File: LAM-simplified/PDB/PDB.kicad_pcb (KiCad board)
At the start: 2 copper layers, 115 x 115 mm, 23 parts, among them J1 2.54mm 2x3, J10 xt60-female, J11 xt60-female, J12 xt60-female, J13 xt90-female, J14 xt90-female, J15 2.54mm 2x3, J2 2.54mm 2x3, J3 2.54mm 2x3, J5 xt30-female, J6 xt30-female, J7 xt60-female, J8 xt60-female, J9 xt60-female

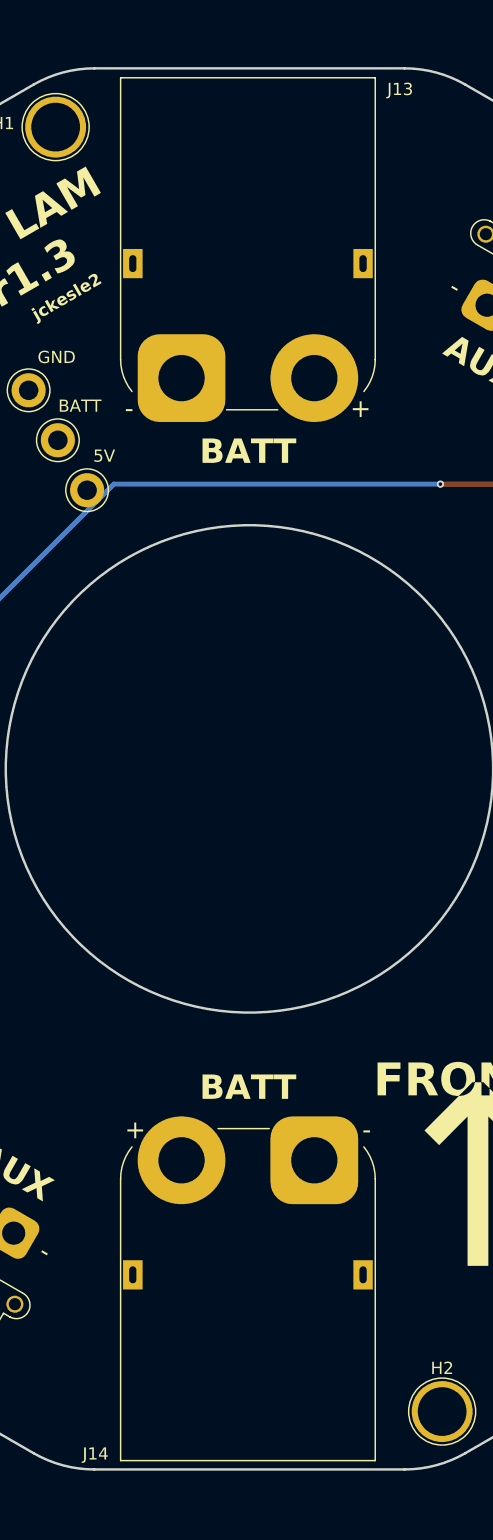
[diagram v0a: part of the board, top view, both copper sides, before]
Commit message: fix XT90-F footprint
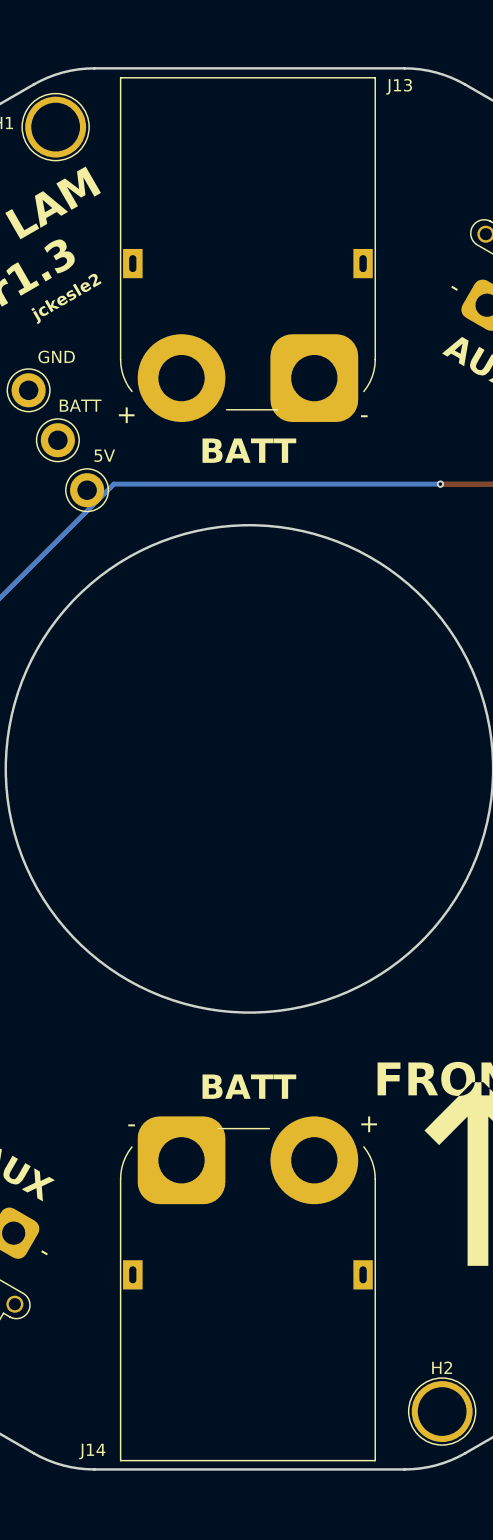
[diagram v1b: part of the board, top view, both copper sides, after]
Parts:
- J13, J14: footprint Connector_AMASS:AMASS_XT90PW-M_1x02_P10.90mm_Horizontal -> aerpaw-footprints:AMASS_XT90PW-F
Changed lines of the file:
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@@
 	(net 10 "unconnected-(J15-Pin_4-Pad4)")
 	(net 11 "unconnected-(J15-Pin_3-Pad3)")
-	(footprint "Connector_AMASS:AMASS_XT90PW-M_1x02_P10.90mm_Horizontal"
+	(footprint "aerpaw-footprints:AMASS_XT90PW-F"
 		(layer "F.Cu")
 		(at 158.25 65.5)
@@
 		(tags "RC")
 		(property "Reference" "J13"
-			(at 17.95 -23.7 0)
+			(at 17.95 -24 0)
 			(layer "F.SilkS")
 			(effects
@@
 			)
 		)
-		(property "Datasheet" "~"
+		(property "Datasheet" ""
 			(at 0 0 0)
 			(unlocked yes)
@@
 			)
 		)
-		(property "Description" "https://www.lcsc.com/product-detail/C3040690.html"
+		(property "Description" ""
 			(at 0 0 0)
 			(unlocked yes)
@@
 		)
 		(fp_text user "-"
-			(at -4.3 2.5 0)
+			(at 15 3 0)
 			(layer "F.SilkS")
 			(effects
@@
 		)
 		(fp_text user "+"
-			(at 14.7 2.5 0)
+			(at -4.5 3 0)
 			(layer "F.SilkS")
 			(effects
@@
 		)
 		(pad "1" thru_hole roundrect
-			(at 0 0)
+			(at 10.899998 0)
 			(size 7.2 7.2)
 			(drill 3.8)
@@
 		)
 		(pad "2" thru_hole circle
-			(at 10.899998 0)
+			(at 0 0)
 			(size 7.2 7.2)
 			(drill 3.8)
@@
 		)
 	)
-	(footprint "Connector_AMASS:AMASS_XT90PW-M_1x02_P10.90mm_Horizontal"
+	(footprint "aerpaw-footprints:AMASS_XT90PW-F"
 		(layer "F.Cu")
 		(at 169.149999 129.7 180)
@@
 		(tags "RC")
 		(property "Reference" "J14"
-			(at 17.949999 -24.1 0)
+			(at 18.149999 -23.8 180)
 			(layer "F.SilkS")
 			(effects
@@
 		)
 		(property "Value" "xt90-female"
-			(at 3.599999 4 0)
-			(layer "F.Fab")
-			(effects
-				(font
-					(size 1 1)
-					(thickness 0.15)
-				)
-			)
-		)
-		(property "Datasheet" "~"
+			(at 3.6 4 180)
+			(layer "F.Fab")
+			(effects
+				(font
+					(size 1 1)
+					(thickness 0.15)
+				)
+			)
+		)
+		(property "Datasheet" ""
 			(at 0 0 180)
 			(unlocked yes)
@@
 			)
 		)
-		(property "Description" "https://www.lcsc.com/product-detail/C3040690.html"
+		(property "Description" ""
 			(at 0 0 180)
 			(unlocked yes)
@@
 			(start 15.9 -1.522958)
 			(mid 15.659164 -0.130586)
-			(end 14.964641 1.099999)
+			(end 14.964641 1.1)
 			(stroke
 				(width 0.12)
@@
 		)
 		(fp_arc
-			(start -4.06464 1.1)
-			(mid -4.759165 -0.130584)
+			(start -4.064641 1.1)
+			(mid -4.759165 -0.130585)
 			(end -5 -1.522958)
 			(stroke
@@
 			(layer "F.SilkS")
 		)
-		(fp_poly
-			(pts
-				(xy -5.449999 -25.1) (xy 16.35 -25.1) (xy 16.35 4.1) (xy -5.45 4.1)
-			)
+		(fp_rect
+			(start -5.45 -25.1)
+			(end 16.35 4.1)
 			(stroke
 				(width 0.05)
@@
 		(fp_line
 			(start 15.85 -24.6)
-			(end 15.85 -1.589999)
+			(end 15.85 -1.59)
 			(stroke
 				(width 0.1)
@@
 		(fp_line
 			(start -0.85 2.51)
-			(end 11.749999 2.51)
+			(end 11.75 2.51)
 			(stroke
 				(width 0.1)
@@
 		)
 		(fp_arc
-			(start 15.85 -1.589999)
+			(start 15.85 -1.59)
 			(mid 14.649138 1.309138)
-			(end 11.749999 2.51)
+			(end 11.75 2.51)
 			(stroke
 				(width 0.1)
@@
 		)
 		(fp_text user "+"
-			(at 14.699999 2.5 0)
+			(at -4.5 3 180)
 			(layer "F.SilkS")
 			(effects
@@
 		)
 		(fp_text user "-"
-			(at -4.3 2.500001 0)
+			(at 15 3 180)
 			(layer "F.SilkS")
 			(effects
@@
 		)
 		(fp_text user "${REFERENCE}"
-			(at 5.449999 -8.499999 0)
+			(at 5.449999 -8.5 180)
 			(layer "F.Fab")
 			(effects
@@
 		)
 		(pad "1" thru_hole roundrect
-			(at 0 0 180)
+			(at 10.899998 0 180)
 			(size 7.2 7.2)
 			(drill 3.8)
@@
 		)
 		(pad "2" thru_hole circle
-			(at 10.899998 0 180)
+			(at 0 0 180)
 			(size 7.2 7.2)
 			(drill 3.8)
@@
 		)
 		(pad "MP" thru_hole rect
-			(at 14.900001 -9.4 180)
+			(at 14.9 -9.4 180)
 			(size 1.6 2.4)
 			(drill oval 0.6 1.4)
